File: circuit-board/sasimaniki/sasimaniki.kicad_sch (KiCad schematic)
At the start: 12 parts, among them J2 Conn_01x02_Socket, J3 Conn_01x03_Socket, J4 Conn_01x05_Pin, U1 AE-ESP32-WROOM-32E-MINI, U2 AE-LXDC55-5V

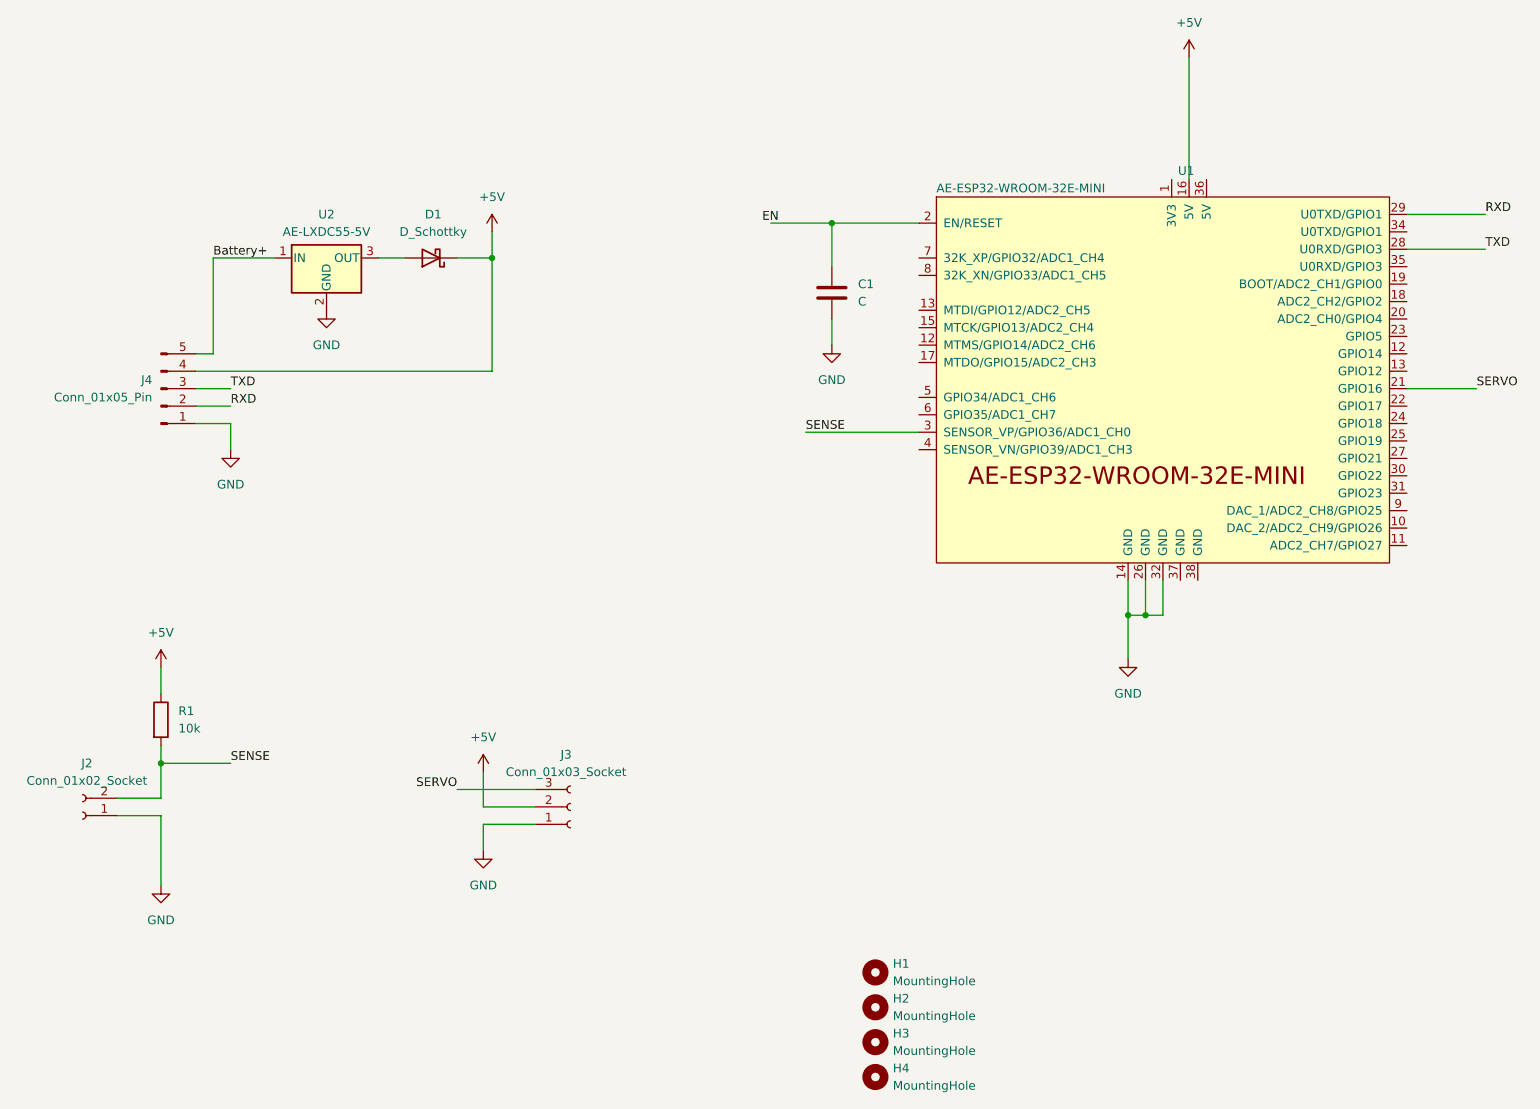
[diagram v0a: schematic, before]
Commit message: update "measure" circuit board.
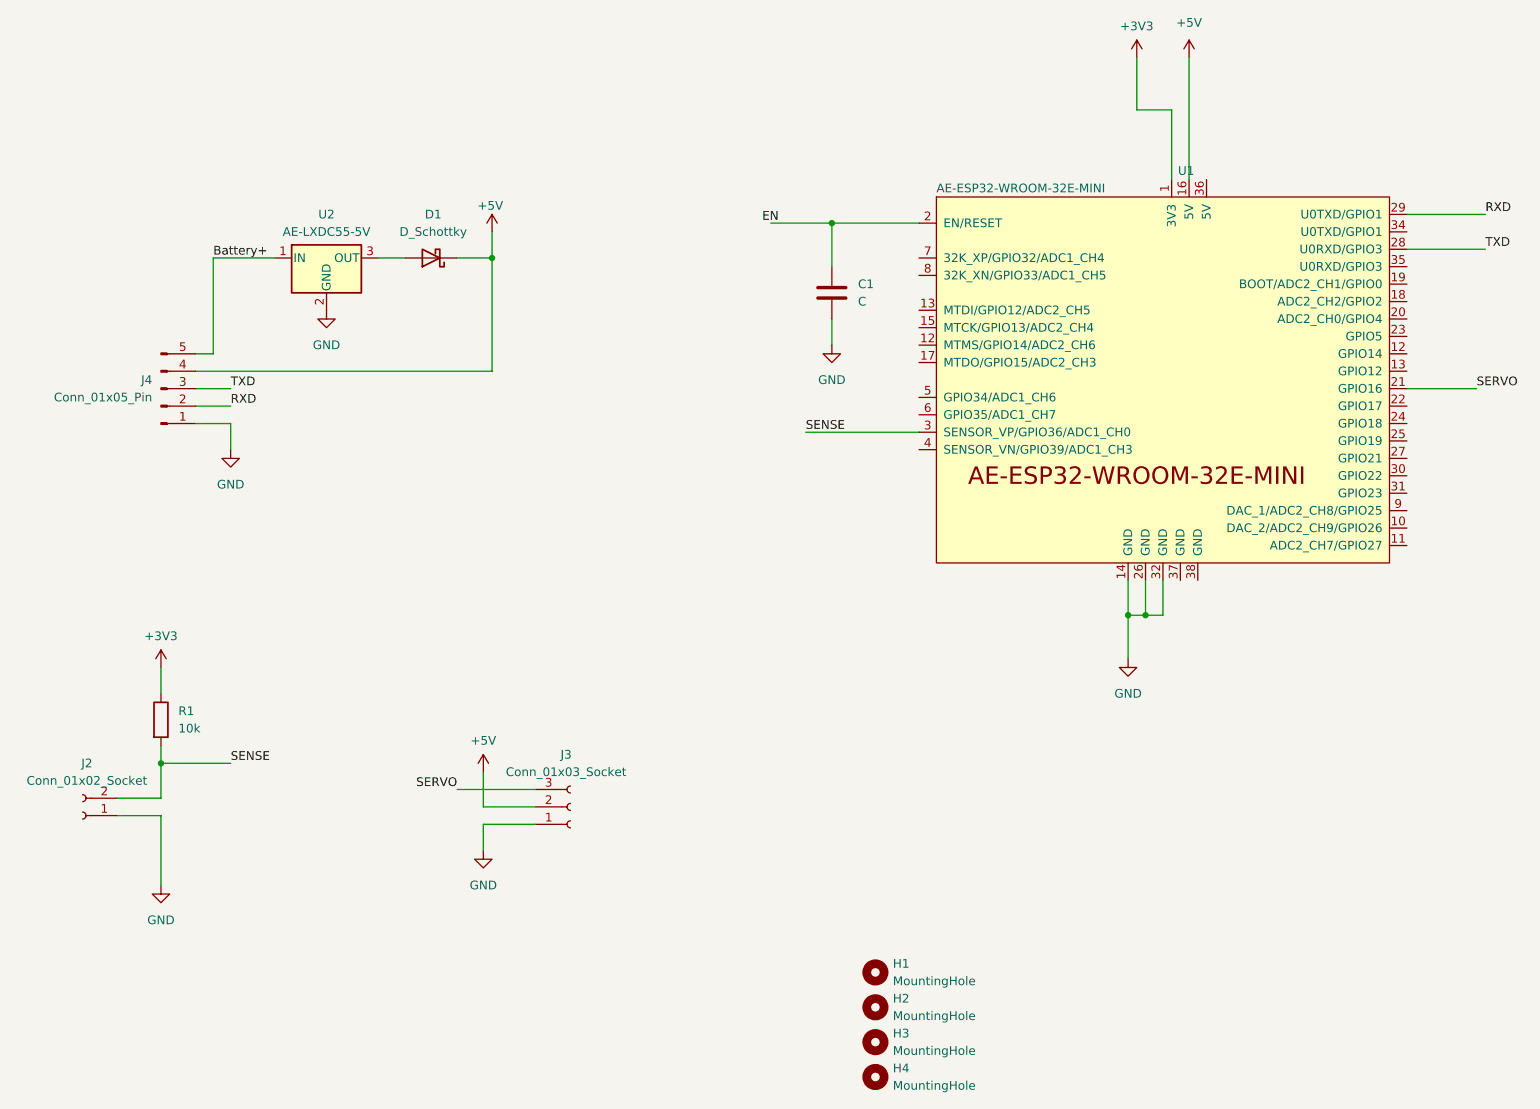
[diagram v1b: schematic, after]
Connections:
- net +5V: no longer R1.1
- net +3V3: now reaches U1.1 (3V3)
- net +3V3: now also R1.1
